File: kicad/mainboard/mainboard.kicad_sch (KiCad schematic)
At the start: 33 parts, among them J1 USB_C_Receptacle_USB2.0_16P, J2 Conn_01x07_Socket, J3 Conn_01x06_Socket, J4 Conn_01x03_Socket, J5 Conn_01x07_Socket, U1 TPD1E05U06DYA, U2 TPD1E05U06DYA, U3 ESP32-S3-WROOM-1, U4 TPD1E05U06DYA, U5 TLV1117-33

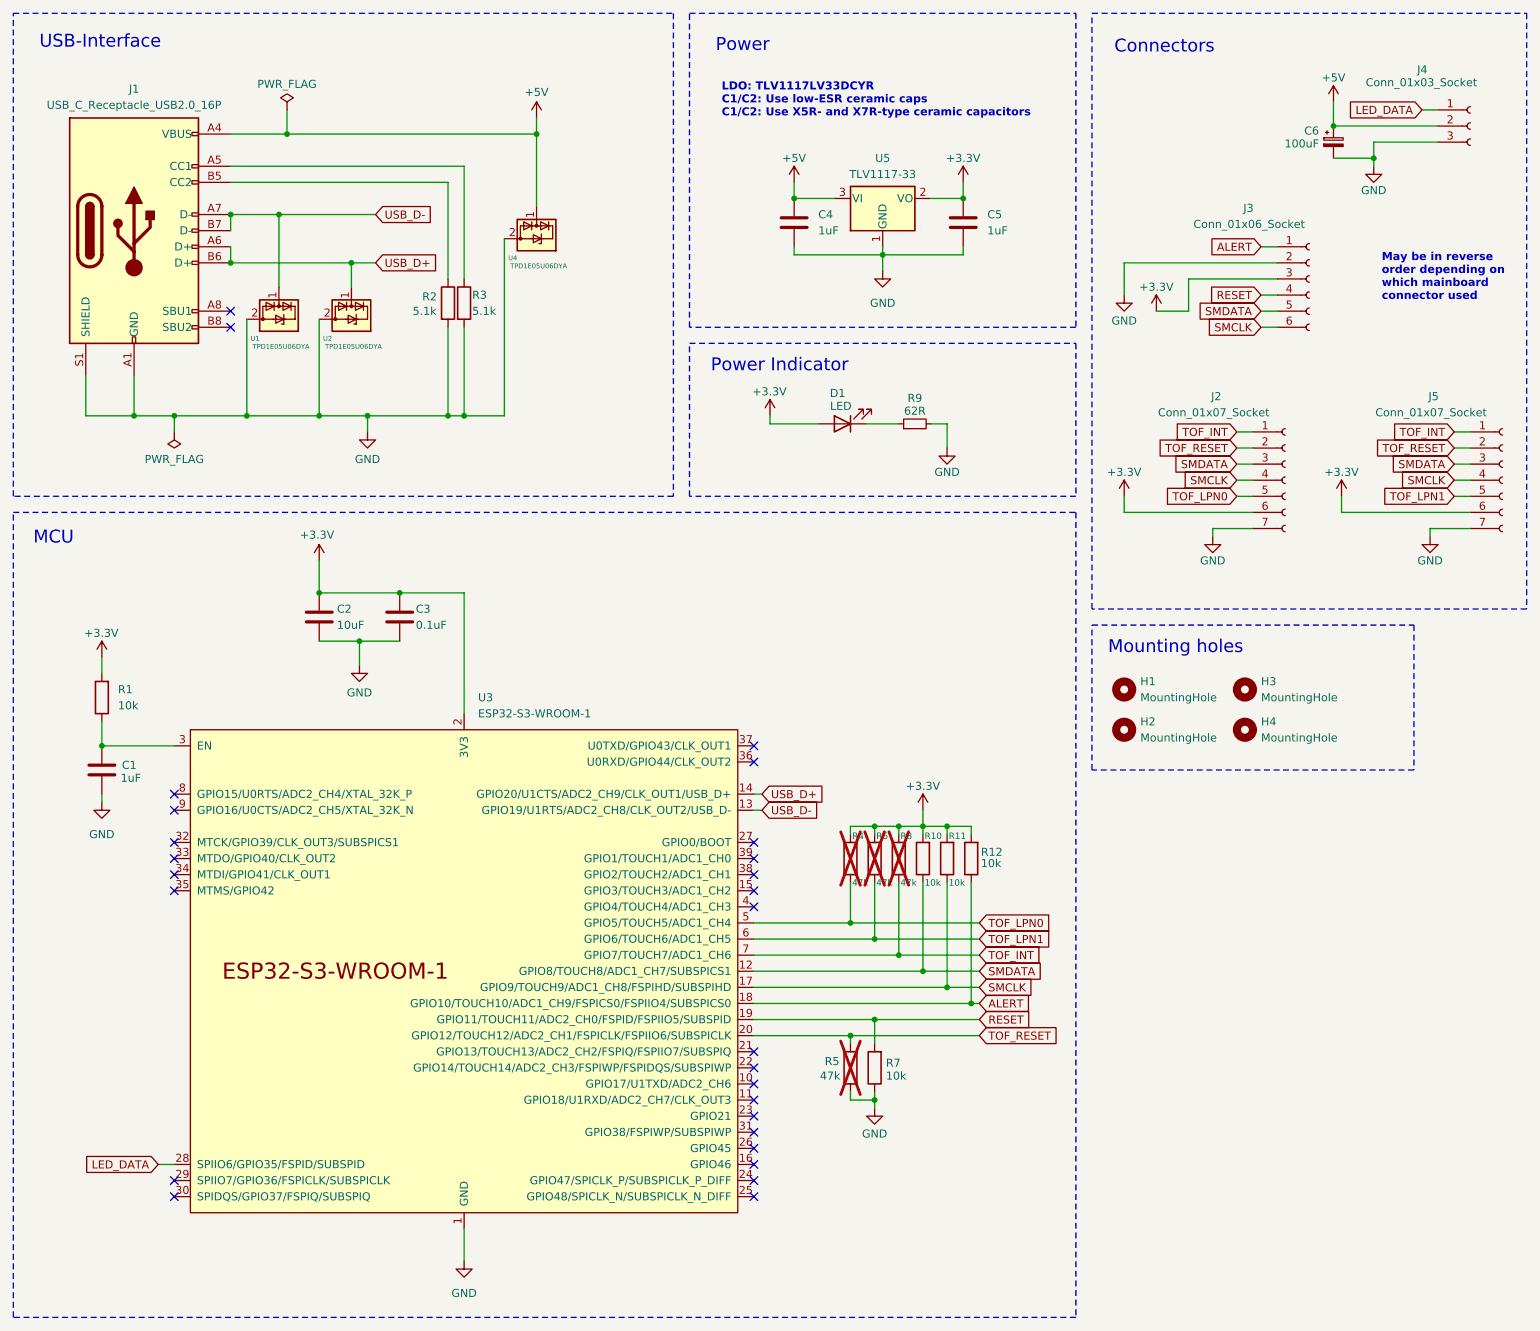
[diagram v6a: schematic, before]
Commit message: v3 mainboard with more tof sensors
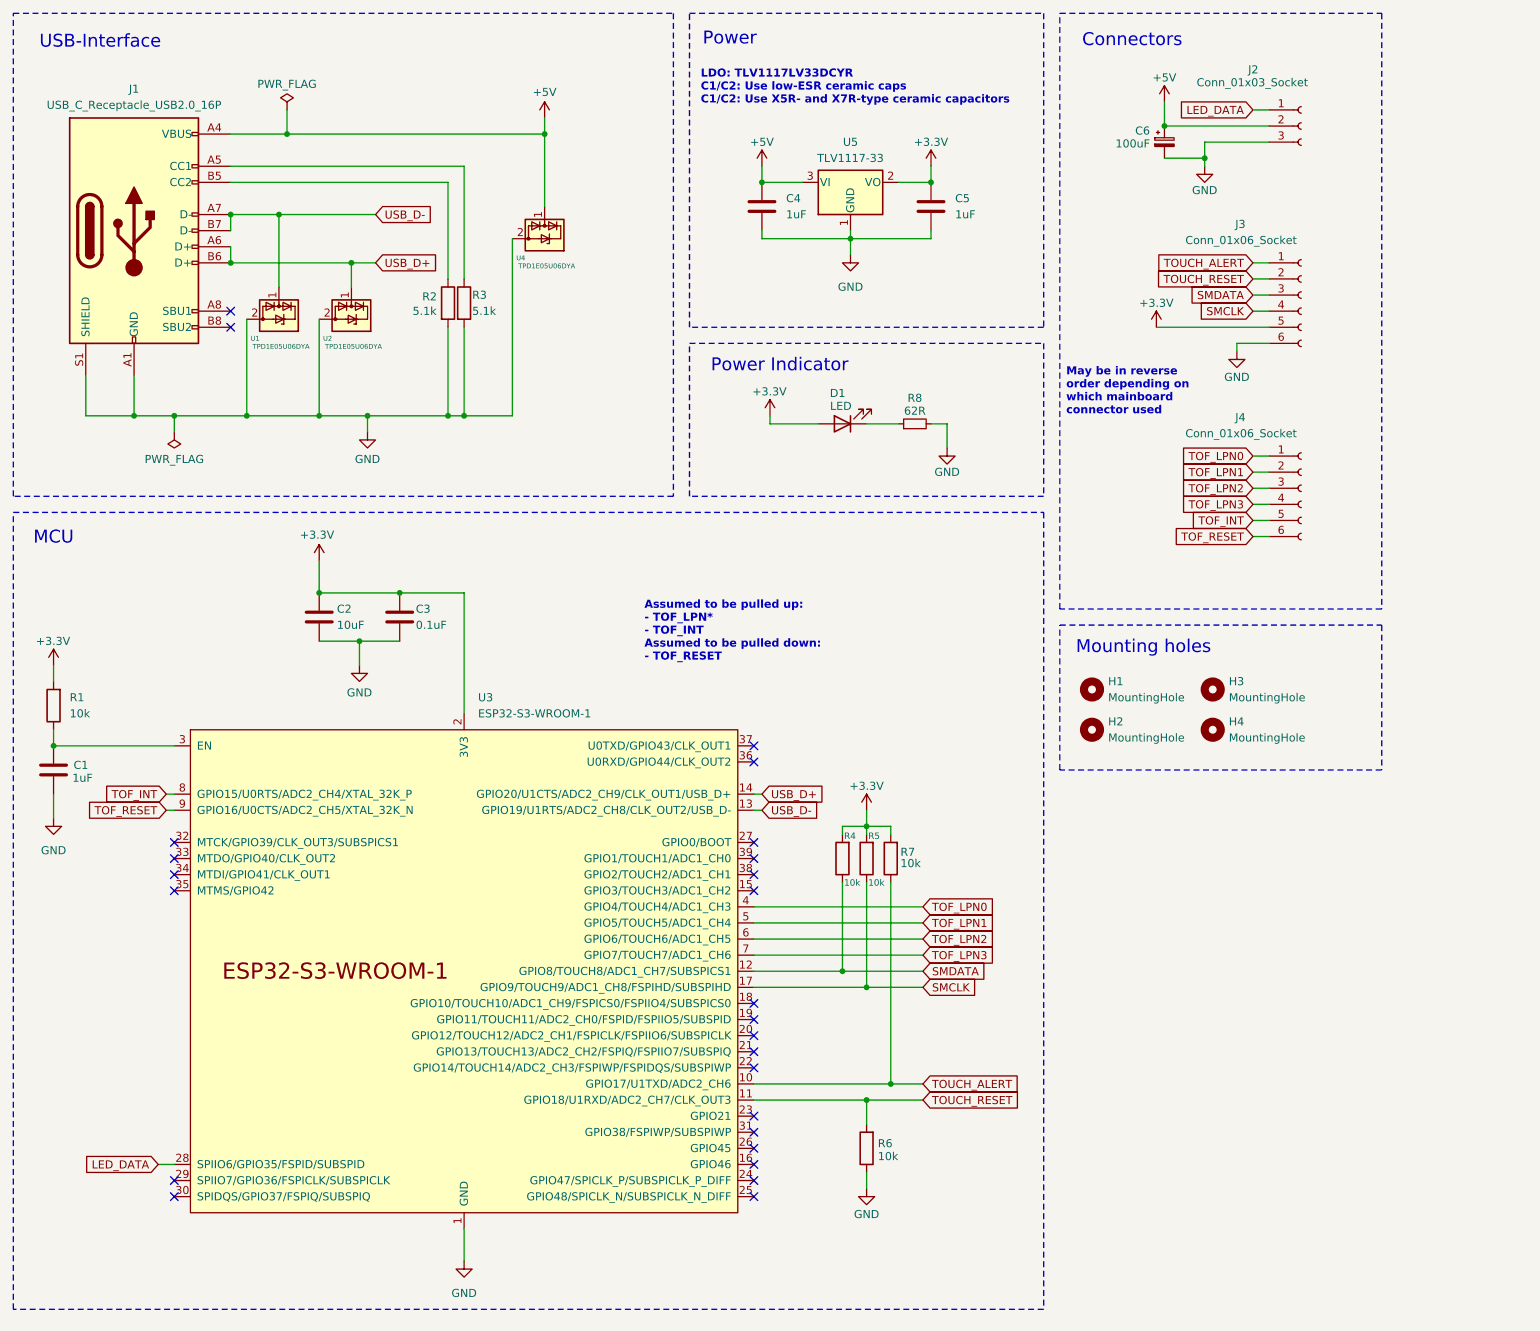
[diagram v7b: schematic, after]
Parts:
- removed J2, J5: Conn_01x07_Socket, Connector_JST:JST_GH_SM07B-GHS-TB_1x07-1MP_P1.25mm_Horizontal, symbol Connector:Conn_01x07_Socket
- removed R4, R5, R6, R8: 47k, Resistor_SMD:R_0805_2012Metric_Pad1.20x1.40mm_HandSolder, symbol Device:R
- added J4: Conn_01x06_Socket, Connector_JST:JST_GH_SM06B-GHS-TB_1x06-1MP_P1.25mm_Horizontal, symbol Connector:Conn_01x06_Socket
- renumbered J4 to J2, R10 to R4, R11 to R5, R7 to R6, R12 to R7, R9 to R8
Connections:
- net +3.3V: now also J3.5 (Pin_5); no longer J3.3 (Pin_3)
- net GND: now also J3.6 (Pin_6); no longer J3.2 (Pin_2)
- net SMCLK: now also J3.4 (Pin_4); no longer J3.6 (Pin_6)
- net SMDATA: now also J3.3 (Pin_3); no longer J3.5 (Pin_5)
- net TOF_INT: now also U3.8 (GPIO15/U0RTS/ADC2_CH4/XTAL_32K_P), J4.5 (Pin_5); no longer U3.7 (GPIO7/TOUCH7/ADC1_CH6)
- net TOF_LPN0: now also U3.4 (GPIO4/TOUCH4/ADC1_CH3), J4.1 (Pin_1); no longer U3.5 (GPIO5/TOUCH5/ADC1_CH4)
- net TOF_LPN1: now also U3.5 (GPIO5/TOUCH5/ADC1_CH4), J4.2 (Pin_2); no longer U3.6 (GPIO6/TOUCH6/ADC1_CH5)
- net TOF_RESET: now also U3.9 (GPIO16/U0CTS/ADC2_CH5/XTAL_32K_N), J4.6 (Pin_6); no longer U3.20 (GPIO12/TOUCH12/ADC2_CH1/FSPICLK/FSPIIO6/SUBSPICLK)
- net TOUCH_ALERT: now reaches U3.10 (GPIO17/U1TXD/ADC2_CH6)
- net TOUCH_ALERT: now also J3.1 (Pin_1), R7.1
- net TOUCH_RESET: now reaches U3.11 (GPIO18/U1RXD/ADC2_CH7/CLK_OUT3)
- net TOUCH_RESET: now also J3.2 (Pin_2), R6.2
- removed net ALERT: J3.1 (Pin_1), R7.1, U3.18 (GPIO10/TOUCH10/ADC1_CH9/FSPICS0/FSPIIO4/SUBSPICS0)
- removed net RESET: J3.4 (Pin_4), R6.2, U3.19 (GPIO11/TOUCH11/ADC2_CH0/FSPID/FSPIIO5/SUBSPID)
- new net TOF_LPN2: J4.3 (Pin_3), U3.6 (GPIO6/TOUCH6/ADC1_CH5)
- new net TOF_LPN3: J4.4 (Pin_4), U3.7 (GPIO7/TOUCH7/ADC1_CH6)
- no-connect marks 27 -> 25
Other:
- note added: "Assumed to be pulled up: - TOF_LPN* - TOF_INT Assumed to be pulled down: - TOF_RESET"
- moved on the sheet: C1, C4, C5, C6, H1, H2, H3, H4, J2, J3, R1, R4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

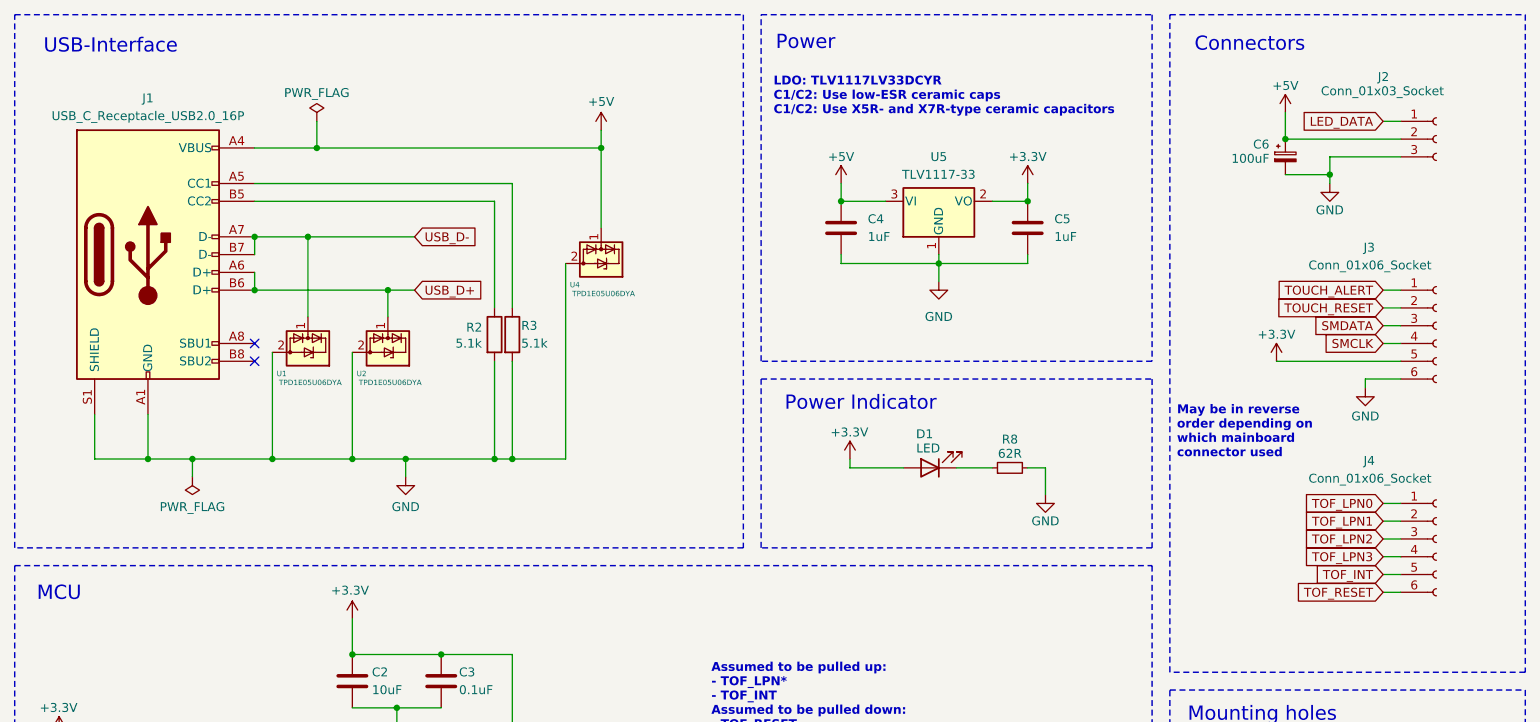
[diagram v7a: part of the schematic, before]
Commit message: update to kicad 9
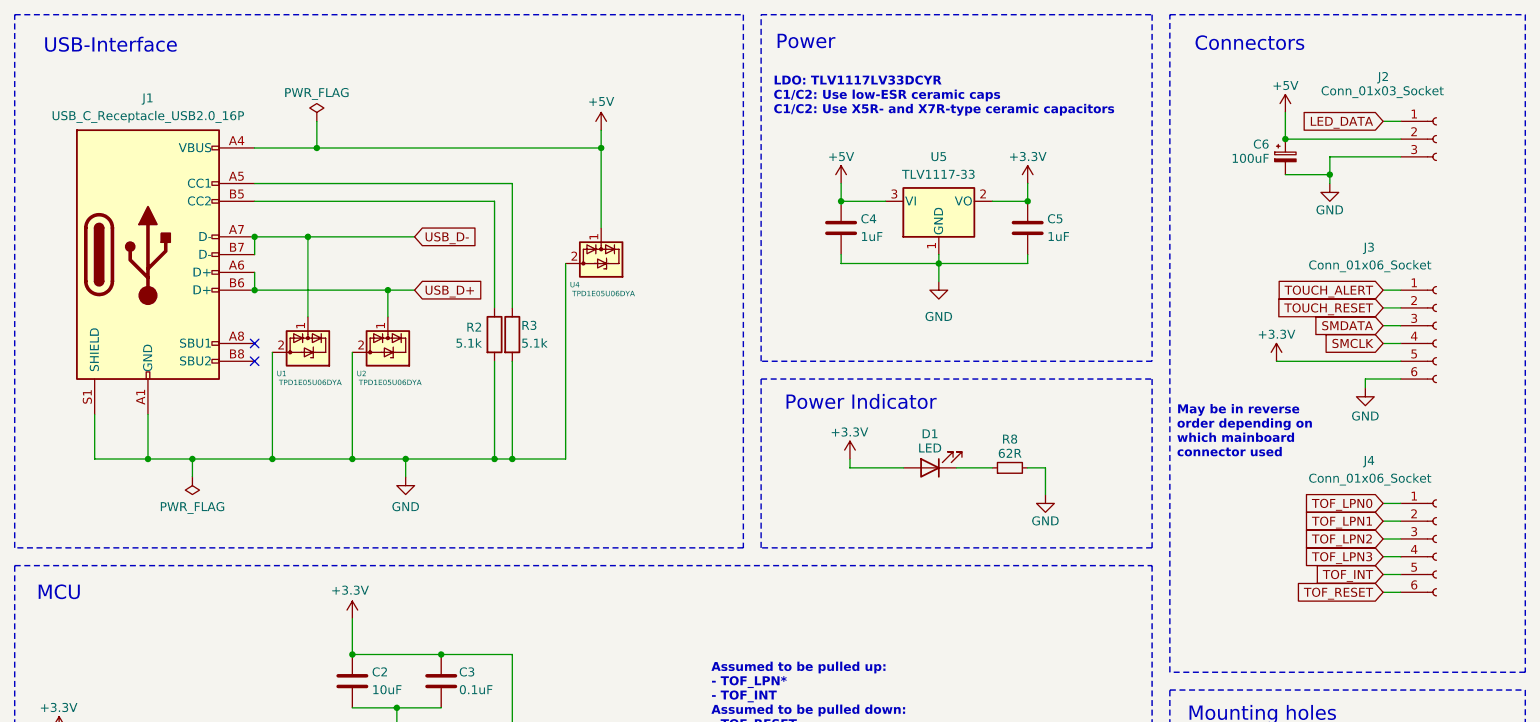
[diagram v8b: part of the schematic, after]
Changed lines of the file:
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@@
 (kicad_sch
-	(version 20231120)
+	(version 20250114)
 	(generator "eeschema")
-	(generator_version "8.0")
+	(generator_version "9.0")
 	(paper "A3")
+	(rectangle
+		(start 15.24 93.98)
+		(end 177.8 219.71)
+		(stroke
+			(width 0.2032)
+			(type dash)
+		)
+		(fill
+			(type none)
+		)
+	)
+	(rectangle
+		(start 15.24 15.24)
+		(end 119.38 91.44)
+		(stroke
+			(width 0.2032)
+			(type dash)
+		)
+		(fill
+			(type none)
+		)
+	)
+	(rectangle
+		(start 121.92 67.31)
+		(end 177.8 91.44)
+		(stroke
+			(width 0.2032)
+			(type dash)
+		)
+		(fill
+			(type none)
+		)
+	)
+	(rectangle
+		(start 180.34 111.76)
+		(end 231.14 134.62)
+		(stroke
+			(width 0.2032)
+			(type dash)
+		)
+		(fill
+			(type none)
+		)
+	)
+	(rectangle
+		(start 180.34 15.24)
+		(end 231.14 109.22)
+		(stroke
+			(width 0.2032)
+			(type dash)
+		)
+		(fill
+			(type none)
+		)
+	)
+	(rectangle
+		(start 121.92 15.24)
+		(end 177.8 64.77)
+		(stroke
+			(width 0.2032)
+			(type dash)
+		)
+		(fill
+			(type none)
+		)
+	)
+	(text "Assumed to be pulled up:\n- TOF_LPN*\n- TOF_INT\nAssumed to be pulled down:\n- TOF_RESET"
+		(exclude_from_sim no)
+		(at 114.808 112.776 0)
+		(effects
+			(font
+				(size 1.27 1.27)
+				(thickness 0.254)
+				(bold yes)
+				(color 251 41 255 1)
+			)
+			(justify left)
+		)
+	)
+	(text "May be in reverse\norder depending on\nwhich mainboard\nconnector used"
+		(exclude_from_sim no)
+		(at 181.356 74.93 0)
+		(effects
+			(font
+				(size 1.27 1.27)
+				(thickness 0.254)
+				(bold yes)
+				(color 251 41 255 1)
+			)
+			(justify left)
+		)
+	)
+	(text "Power Indicator"
+		(exclude_from_sim no)
+		(at 136.144 70.866 0)
+		(effects
+			(font
+				(size 2.032 2.032)
+			)
+		)
+	)
+	(text "Connectors"
+		(exclude_from_sim no)
+		(at 191.77 19.558 0)
+		(effects
+			(font
+				(size 2.032 2.032)
+			)
+		)
+	)
+	(text "MCU"
+		(exclude_from_sim no)
+		(at 21.59 98.044 0)
+		(effects
+			(font
+				(size 2.032 2.032)
+			)
+		)
+	)
+	(text "LDO: TLV1117LV33DCYR\nC1/C2: Use low-ESR ceramic caps\nC1/C2: Use X5R- and X7R-type ceramic capacitors"
+		(exclude_from_sim no)
+		(at 123.698 26.924 0)
+		(effects
+			(font
+				(size 1.27 1.27)
+				(thickness 0.254)
+				(bold yes)
+				(color 251 41 255 1)
+			)
+			(justify left)
+		)
+	)
+	(text "Mounting holes"
+		(exclude_from_sim no)
+		(at 193.548 115.316 0)
+		(effects
+			(font
+				(size 2.032 2.032)
+			)
+		)
+	)
+	(text "USB-Interface"
+		(exclude_from_sim no)
+		(at 28.956 19.812 0)
+		(effects
+			(font
+				(size 2.032 2.032)
+			)
+		)
+	)
+	(text "Power"
+		(exclude_from_sim no)
+		(at 128.27 19.304 0)
+		(effects
+			(font
+				(size 2.032 2.032)
+			)
+		)
+	)
 	(junction
 		(at 133.35 41.91)
@@
 		)
 	)
-	(rectangle
-		(start 15.24 93.98)
-		(end 177.8 219.71)
-		(stroke
-			(width 0.2032)
-			(type dash)
-		)
-		(fill
-			(type none)
-		)
-	)
-	(rectangle
-		(start 15.24 15.24)
-		(end 119.38 91.44)
-		(stroke
-			(width 0.2032)
-			(type dash)
-		)
-		(fill
-			(type none)
-		)
-	)
-	(rectangle
-		(start 121.92 67.31)
-		(end 177.8 91.44)
-		(stroke
-			(width 0.2032)
-			(type dash)
-		)
-		(fill
-			(type none)
-		)
-	)
-	(rectangle
-		(start 180.34 111.76)
-		(end 231.14 134.62)
-		(stroke
-			(width 0.2032)
-			(type dash)
-		)
-		(fill
-			(type none)
-		)
-	)
-	(rectangle
-		(start 180.34 15.24)
-		(end 231.14 109.22)
-		(stroke
-			(width 0.2032)
-			(type dash)
-		)
-		(fill
-			(type none)
-		)
-	)
-	(rectangle
-		(start 121.92 15.24)
-		(end 177.8 64.77)
-		(stroke
-			(width 0.2032)
-			(type dash)
-		)
-		(fill
-			(type none)
-		)
-	)
-	(text "Assumed to be pulled up:\n- TOF_LPN*\n- TOF_INT\nAssumed to be pulled down:\n- TOF_RESET"
-		(exclude_from_sim no)
-		(at 114.808 112.776 0)
-		(effects
-			(font
-				(size 1.27 1.27)
-				(thickness 0.254)
-				(bold yes)
-				(color 251 41 255 1)
-			)
-			(justify left)
-		)
-	)
-	(text "May be in reverse\norder depending on\nwhich mainboard\nconnector used"
-		(exclude_from_sim no)
-		(at 181.356 74.93 0)
-		(effects
-			(font
-				(size 1.27 1.27)
-				(thickness 0.254)
-				(bold yes)
-				(color 251 41 255 1)
-			)
-			(justify left)
-		)
-	)
-	(text "Power Indicator"
-		(exclude_from_sim no)
-		(at 136.144 70.866 0)
-		(effects
-			(font
-				(size 2.032 2.032)
-			)
-		)
-	)
-	(text "Connectors"
-		(exclude_from_sim no)
-		(at 191.77 19.558 0)
-		(effects
-			(font
-				(size 2.032 2.032)
-			)
-		)
-	)
-	(text "MCU"
-		(exclude_from_sim no)
-		(at 21.59 98.044 0)
-		(effects
-			(font
-				(size 2.032 2.032)
-			)
-		)
-	)
-	(text "LDO: TLV1117LV33DCYR\nC1/C2: Use low-ESR ceramic caps\nC1/C2: Use X5R- and X7R-type ceramic capacitors"
-		(exclude_from_sim no)
-		(at 123.698 26.924 0)
-		(effects
-			(font
-				(size 1.27 1.27)
-				(thickness 0.254)
-				(bold yes)
-				(color 251 41 255 1)
-			)
-			(justify left)
-		)
-	)
-	(text "Mounting holes"
-		(exclude_from_sim no)
-		(at 193.548 115.316 0)
-		(effects
-			(font
-				(size 2.032 2.032)
-			)
-		)
-	)
-	(text "USB-Interface"
-		(exclude_from_sim no)
-		(at 28.956 19.812 0)
-		(effects
-			(font
-				(size 2.032 2.032)
-			)
-		)
-	)
-	(text "Power"
-		(exclude_from_sim no)
-		(at 128.27 19.304 0)
-		(effects
-			(font
-				(size 2.032 2.032)
-			)
-		)
-	)
 	(global_label "TOF_LPN2"
 		(shape input)
@@
 		(dnp no)
 		(property "Reference" "D1"
-			(at 145.288 75.184 0)
+			(at 146.05 75.184 0)
 			(effects
 				(font
@@
 		)
 		(property "Value" "LED"
-			(at 145.796 77.216 0)
+			(at 146.05 77.216 0)
 			(effects
 				(font
@@
 			)
 		)
+		(property "Sim.Pins" "1=K 2=A"
+			(at 146.05 80.01 0)
+			(effects
+				(font
+					(size 1.27 1.27)
+				)
+				(hide yes)
+			)
+		)
 		(pin "2"
 		)
@@
 		(dnp no)
 		(property "Reference" "C4"
-			(at 137.16 44.4499 0)
+			(at 136.144 44.45 0)
 			(effects
 				(font
@@
 		)
 		(property "Value" "1uF"
-			(at 137.16 46.9899 0)
+			(at 136.144 46.99 0)
 			(effects
 				(font
@@
 		(on_board yes)
 		(dnp no)
-		(fields_autoplaced yes)
 		(property "Reference" "C5"
-			(at 163.83 44.4499 0)
+			(at 162.814 44.45 0)
 			(effects
 				(font
@@
 		)
 		(property "Value" "1uF"
-			(at 163.83 46.9899 0)
+			(at 162.814 46.99 0)
 			(effects
 				(font
@@
 		)
 	)
+	(embedded_fonts no)
 )
